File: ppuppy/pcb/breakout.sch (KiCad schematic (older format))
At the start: 48 parts, among them Q1 2N3904, Q2 2N3904, Q3 2N3904, Q4 2N3904, Q5 2N3904, Q6 2N3904, Q7 2N3904, Q8 2N3904

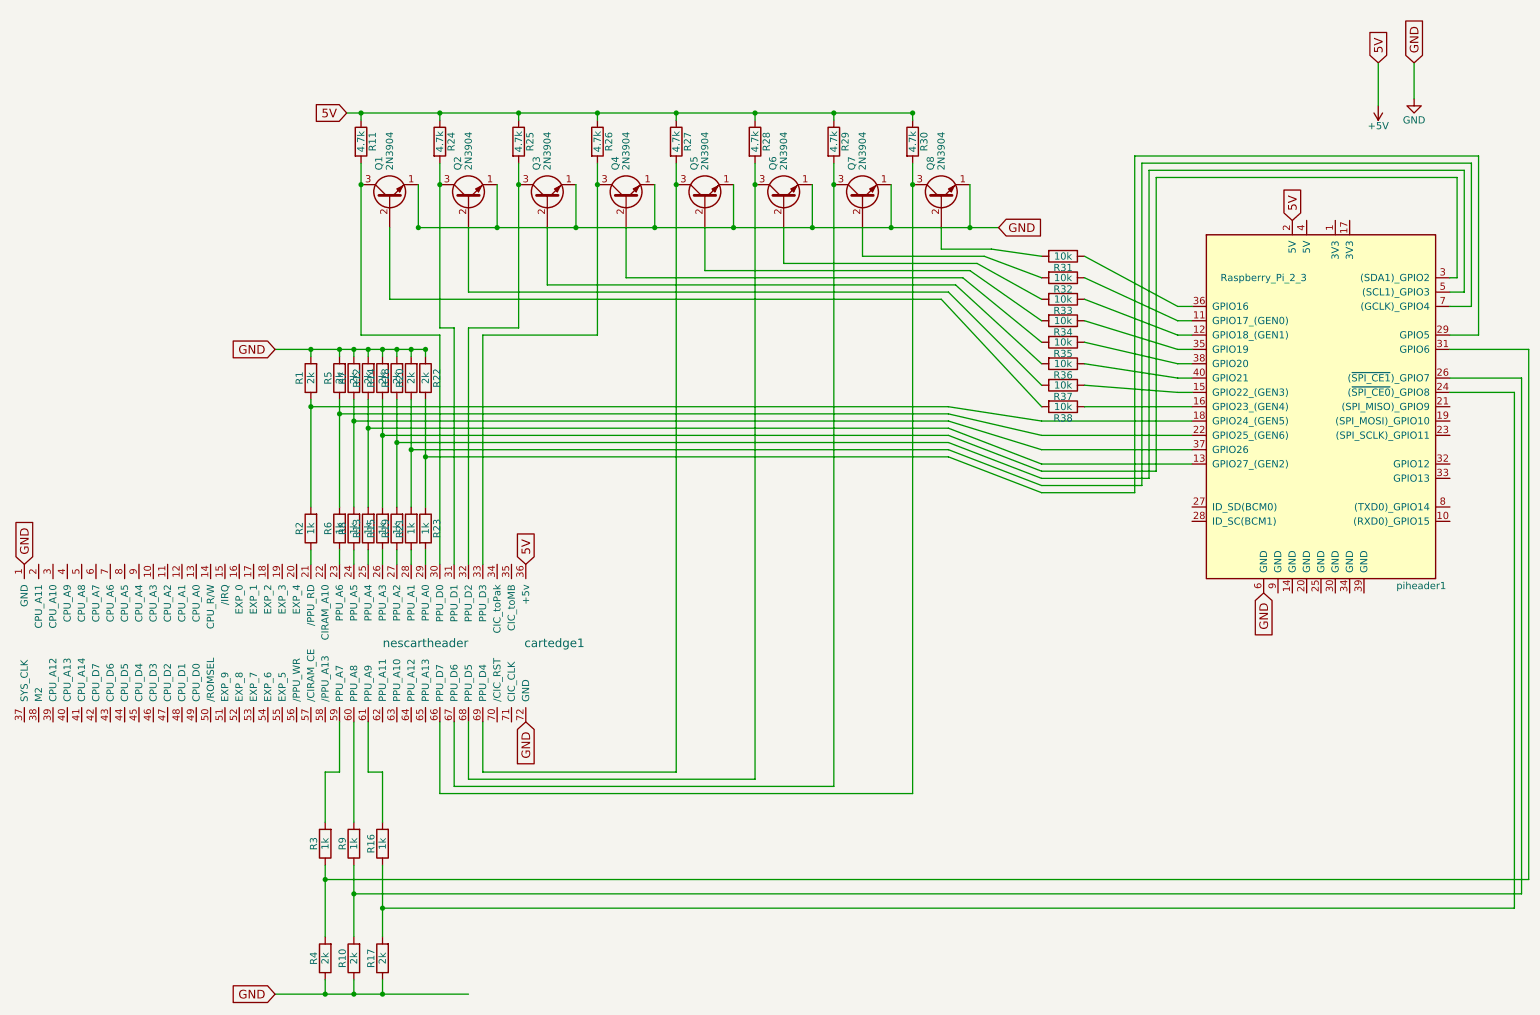
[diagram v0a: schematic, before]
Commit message: new breakout with eeprom and headers
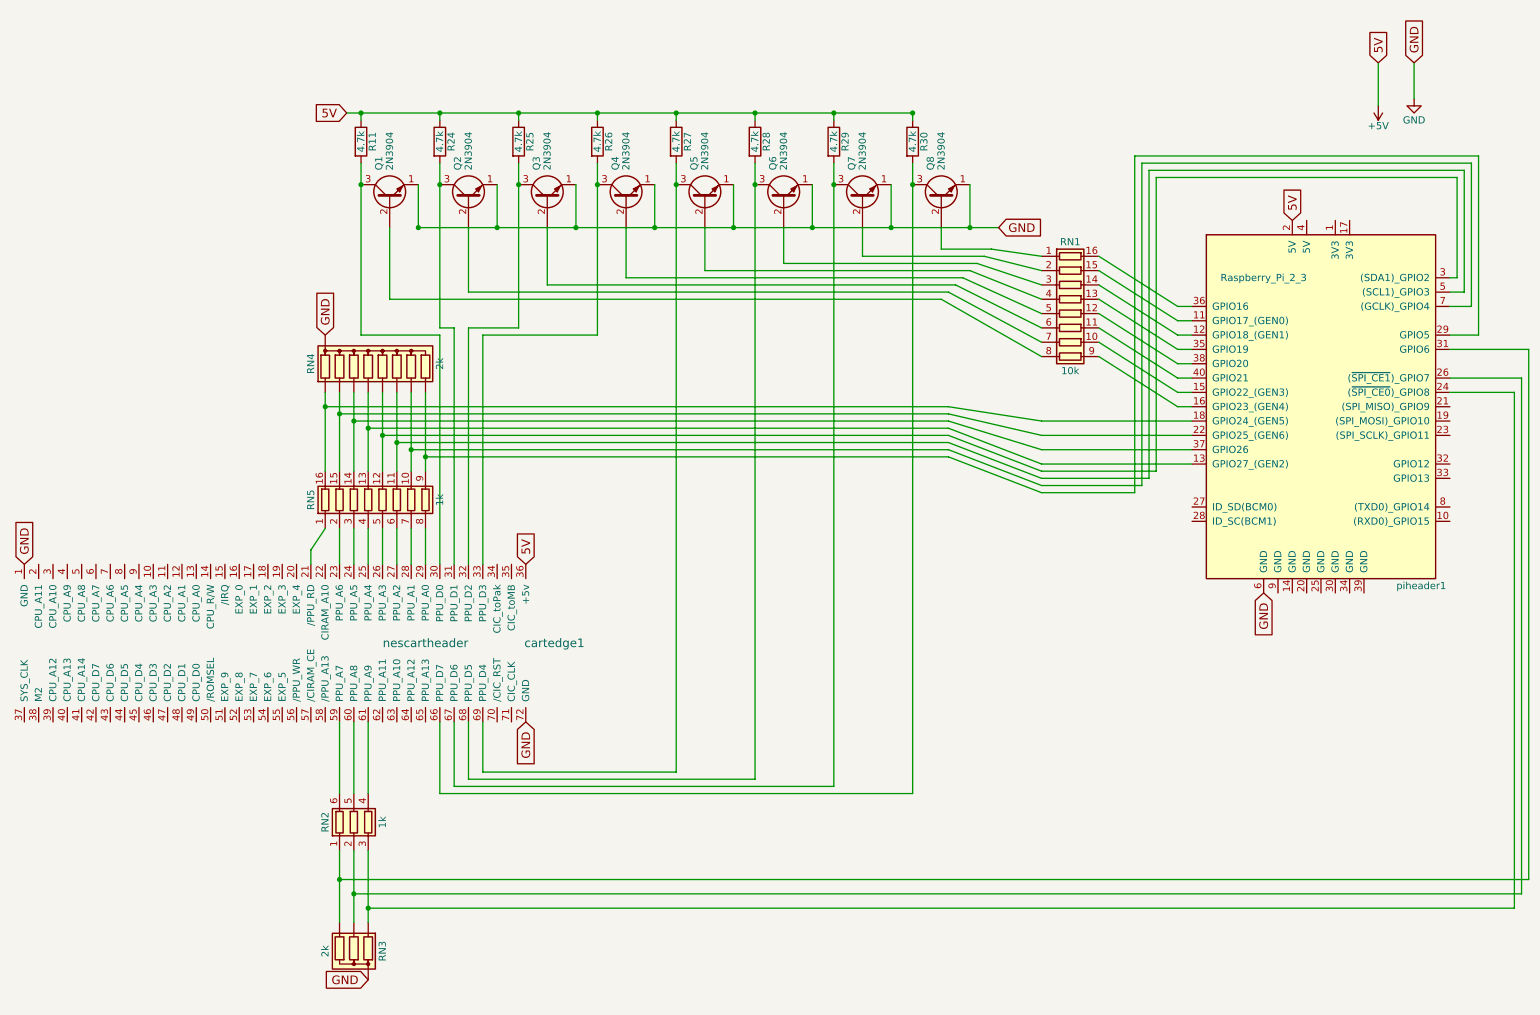
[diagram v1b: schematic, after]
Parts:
- removed R1, R10, R12, R14, R17, R18, R20, R22, R4, R5, R7: 2k, symbol R
- removed R13, R15, R16, R19, R2, R21, R23, R3, R6, R8, R9: 1k, symbol R
- removed R31, R32, R33, R34, R35, R36, R37, R38: 10k, symbol R
- added RN1: 10k, Housings_DIP:DIP-16_W7.62mm, symbol R_Pack08
- added RN2: 1k, Housings_DIP:DIP-6_W10.16mm, symbol R_Pack03
- added RN3: 2k, Resistors_THT:R_Array_SIP4, symbol R_Network03
- added RN4: 2k, Resistors_THT:R_Array_SIP9, symbol R_Network08
- added RN5: 1k, Housings_DIP:DIP-16_W10.16mm, symbol R_Pack08
- Q1, Q2, Q3, Q4, Q5, Q6, Q7, Q8: footprint TO_SOT_Packages_THT:TO-92_Molded_Narrow -> TO_SOT_Packages_THT:TO-92_Molded_Wide
- R11, R24, R25, R26, R27, R28, R29, R30: footprint (none) -> Resistors_THT:R_Axial_DIN0309_L9.0mm_D3.2mm_P25.40mm_Horizontal
- cartedge1: footprint (none) -> footprints:cartedge
- piheader1: footprint Pin_Headers:Pin_Header_Straight_2x20 -> Pin_Headers:Pin_Header_Straight_2x20_Pitch2.54mm
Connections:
- net GND: now also RN3.1 (common), RN4.1 (common)
- net at piheader1.11 (GPIO17_(GEN0)): now also RN1.15 (R2.2)
- net at piheader1.12 (GPIO18_(GEN1)): now also RN1.14 (R3.2)
- net at piheader1.13 (GPIO27_(GEN2)): now also RN4.5 (R4), RN5.13 (R4.2)
- net at piheader1.15 (GPIO22_(GEN3)): now also RN1.10 (R7.2)
- net at piheader1.16 (GPIO23_(GEN4)): now also RN1.9 (R8.2)
- net at piheader1.18 (GPIO24_(GEN5)): now also RN4.2 (R1), RN5.16 (R1.2)
- net at piheader1.22 (GPIO25_(GEN6)): now also RN4.3 (R2), RN5.15 (R2.2)
- net at piheader1.24 ((~SPI_CE0~)_GPIO8): now also RN2.3 (R3.1), RN3.2 (R1)
- net at piheader1.26 ((~SPI_CE1~)_GPIO7): now also RN2.2 (R2.1), RN3.3 (R2)
- net at piheader1.29 (GPIO5): now also RN4.9 (R8), RN5.9 (R8.2)
- net at piheader1.3 ((SDA1)_GPIO2): now also RN4.6 (R5), RN5.12 (R5.2)
- net at piheader1.31 (GPIO6): now also RN2.1 (R1.1), RN3.4 (R3)
- net at piheader1.35 (GPIO19): now also RN1.13 (R4.2)
- net at piheader1.36 (GPIO16): now also RN1.16 (R1.2)
- net at piheader1.37 (GPIO26): now also RN4.4 (R3), RN5.14 (R3.2)
- net at piheader1.38 (GPIO20): now also RN1.12 (R5.2)
- net at piheader1.40 (GPIO21): now also RN1.11 (R6.2)
- net at piheader1.5 ((SCL1)_GPIO3): now also RN4.7 (R6), RN5.11 (R6.2)
- net at piheader1.7 ((GCLK)_GPIO4): now also RN4.8 (R7), RN5.10 (R7.2)
- net at cartedge1.21 (/PPU_RD): now also RN5.1 (R1.1)
- net at cartedge1.23 (PPU_A6): now also RN5.2 (R2.1)
- net at cartedge1.24 (PPU_A5): now also RN5.3 (R3.1)
- net at cartedge1.25 (PPU_A4): now also RN5.4 (R4.1)
- net at cartedge1.26 (PPU_A3): now also RN5.5 (R5.1)
- net at cartedge1.27 (PPU_A2): now also RN5.6 (R6.1)
- net at cartedge1.28 (PPU_A1): now also RN5.7 (R7.1)
- net at cartedge1.29 (PPU_A0): now also RN5.8 (R8.1)
- net at cartedge1.59 (PPU_A7): now also RN2.6 (R1.2)
- net at cartedge1.60 (PPU_A8): now also RN2.5 (R2.2)
- net at cartedge1.61 (PPU_A9): now also RN2.4 (R3.2)
- net at Q1.2 (B): now also RN1.8 (R8.1)
- net at Q2.2 (B): now also RN1.7 (R7.1)
- net at Q3.2 (B): now also RN1.6 (R6.1)
- net at Q4.2 (B): now also RN1.5 (R5.1)
- net at Q5.2 (B): now also RN1.4 (R4.1)
- net at Q6.2 (B): now also RN1.3 (R3.1)
- net at Q7.2 (B): now also RN1.2 (R2.1)
- net at Q8.2 (B): now also RN1.1 (R1.1)
